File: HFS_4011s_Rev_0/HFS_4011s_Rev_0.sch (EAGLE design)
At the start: 56 parts, among them IC1 CP2104, J1 2X06, J2 2X12, J3 1X02, Q1 mmbt2222, Q2 mmbt2222, Q3 MMUN2133LT1G, SW2 KMR2, U1 TPS61090RSAR, U2 MCP73831T-2ACI/OT, U3 AD5693R, U4 LM3671MF-3.3/NOPB, X2 ESP32_WROOM32_SKINNY

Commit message: Added labels for FPAA IO. Still determining peripherals.
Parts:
- added J5: 1X02, HFS4011sCustom:1X02
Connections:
- new net E0: J2.23
- new net E1: J2.21
- new net E2: J2.19
- new net E3: J2.12
- new net E4: J2.10
- new net N$27: J2.14
- new net N$28: J2.16
- new net N$29: J2.18
- new net N$39: J2.13
- new net N$40: J2.15
- new net N$41: J2.17
- new net S0: J2.8
- new net S1: J1.8, J2.6
- new net S2: J2.4
- new net S3: J1.10, J2.2
- new net S4: J2.11
- new net S5: J1.12, J2.9
- new net S6: J2.7
- new net S7: J2.5
- new net S8: J2.3
- new net S9: J2.1
- new net W1: J2.24
- new net W3: J2.22
- new net W4: J2.20
- net 5.0V: now also J5.1
- net GND: now also J5.2
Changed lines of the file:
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@@
 <part name="R16" library="rcl" library_urn="urn:adsk.eagle:library:334" deviceset="R-US_" device="R0603" package3d_urn="urn:adsk.eagle:package:23555/2" value="5.1k"/>
 <part name="U$52" library="microbuilder" deviceset="3.3V" device=""/>
+<part name="J5" library="HFS4011sCustom" deviceset="1X02" device=""/>
+<part name="U$53" library="microbuilder" deviceset="5.0V" device=""/>
+<part name="U$54" library="microbuilder" deviceset="GND" device=""/>
 </parts>
 <sheets>
@@
 <instance part="R16" gate="G$1" x="190.5" y="195.58" rot="R90"/>
 <instance part="U$52" gate="G$1" x="142.24" y="177.8"/>
+<instance part="J5" gate="G$1" x="335.28" y="157.48"/>
+<instance part="U$53" gate="G$1" x="327.66" y="165.1"/>
+<instance part="U$54" gate="G$1" x="327.66" y="152.4"/>
 </instances>
 <busses>
@@
 <pinref part="U$50" gate="G$1" pin="GND"/>
 <wire x1="233.68" y1="129.54" x2="233.68" y2="127" width="0.1524" layer="91"/>
+</segment>
+<segment>
+<pinref part="J5" gate="G$1" pin="2"/>
+<pinref part="U$54" gate="G$1" pin="GND"/>
+<wire x1="330.2" y1="157.48" x2="327.66" y2="157.48" width="0.1524" layer="91"/>
+<wire x1="327.66" y1="157.48" x2="327.66" y2="154.94" width="0.1524" layer="91"/>
 </segment>
 </net>
@@
 <pinref part="C7" gate="G$1" pin="+"/>
 </segment>
+<segment>
+<pinref part="U$53" gate="G$1" pin="5.0V"/>
+<wire x1="327.66" y1="162.56" x2="327.66" y2="160.02" width="0.1524" layer="91"/>
+<pinref part="J5" gate="G$1" pin="1"/>
+<wire x1="327.66" y1="160.02" x2="330.2" y2="160.02" width="0.1524" layer="91"/>
+</segment>
 </net>
 <net name="N$10" class="0">
@@
 </segment>
 </net>
+<net name="S5" class="0">
+<segment>
+<pinref part="J1" gate="J$1" pin="12"/>
+<wire x1="327.66" y1="119.38" x2="335.28" y2="119.38" width="0.1524" layer="91"/>
+<label x="335.28" y="119.38" size="1.778" layer="95"/>
+<wire x1="335.28" y1="119.38" x2="337.82" y2="119.38" width="0.1524" layer="91"/>
+</segment>
+<segment>
+<pinref part="J2" gate="J$1" pin="9"/>
+<wire x1="337.82" y1="96.52" x2="327.66" y2="96.52" width="0.1524" layer="91"/>
+<label x="327.66" y="96.52" size="1.778" layer="95"/>
+</segment>
+</net>
+<net name="S3" class="0">
+<segment>
+<pinref part="J1" gate="J$1" pin="10"/>
+<wire x1="327.66" y1="121.92" x2="332.74" y2="121.92" width="0.1524" layer="91"/>
+<label x="335.28" y="121.92" size="1.778" layer="95"/>
+<wire x1="332.74" y1="121.92" x2="337.82" y2="121.92" width="0.1524" layer="91"/>
+</segment>
+<segment>
+<pinref part="J2" gate="J$1" pin="2"/>
+<wire x1="345.44" y1="106.68" x2="355.6" y2="106.68" width="0.1524" layer="91"/>
+<label x="353.06" y="106.68" size="1.778" layer="95"/>
+</segment>
+</net>
+<net name="S1" class="0">
+<segment>
+<pinref part="J1" gate="J$1" pin="8"/>
+<wire x1="327.66" y1="124.46" x2="332.74" y2="124.46" width="0.1524" layer="91"/>
+<label x="335.28" y="124.46" size="1.778" layer="95"/>
+<wire x1="332.74" y1="124.46" x2="337.82" y2="124.46" width="0.1524" layer="91"/>
+</segment>
+<segment>
+<pinref part="J2" gate="J$1" pin="6"/>
+<wire x1="345.44" y1="101.6" x2="355.6" y2="101.6" width="0.1524" layer="91"/>
+<label x="353.06" y="101.6" size="1.778" layer="95"/>
+</segment>
+</net>
+<net name="S2" class="0">
+<segment>
+<pinref part="J2" gate="J$1" pin="4"/>
+<wire x1="345.44" y1="104.14" x2="355.6" y2="104.14" width="0.1524" layer="91"/>
+<label x="353.06" y="104.14" size="1.778" layer="95"/>
+</segment>
+</net>
+<net name="S0" class="0">
+<segment>
+<pinref part="J2" gate="J$1" pin="8"/>
+<wire x1="345.44" y1="99.06" x2="355.6" y2="99.06" width="0.1524" layer="91"/>
+<label x="353.06" y="99.06" size="1.778" layer="95"/>
+</segment>
+</net>
+<net name="E4" class="0">
+<segment>
+<pinref part="J2" gate="J$1" pin="10"/>
+<wire x1="345.44" y1="96.52" x2="355.6" y2="96.52" width="0.1524" layer="91"/>
+<label x="353.06" y="96.52" size="1.778" layer="95"/>
+</segment>
+</net>
+<net name="E3" class="0">
+<segment>
+<pinref part="J2" gate="J$1" pin="12"/>
+<wire x1="345.44" y1="93.98" x2="355.6" y2="93.98" width="0.1524" layer="91"/>
+<label x="353.06" y="93.98" size="1.778" layer="95"/>
+</segment>
+</net>
+<net name="N$27" class="0">
+<segment>
+<pinref part="J2" gate="J$1" pin="14"/>
+<wire x1="345.44" y1="91.44" x2="355.6" y2="91.44" width="0.1524" layer="91"/>
+</segment>
+</net>
+<net name="N$28" class="0">
+<segment>
+<pinref part="J2" gate="J$1" pin="16"/>
+<wire x1="345.44" y1="88.9" x2="355.6" y2="88.9" width="0.1524" layer="91"/>
+</segment>
+</net>
+<net name="N$29" class="0">
+<segment>
+<pinref part="J2" gate="J$1" pin="18"/>
+<wire x1="345.44" y1="86.36" x2="355.6" y2="86.36" width="0.1524" layer="91"/>
+</segment>
+</net>
+<net name="W4" class="0">
+<segment>
+<pinref part="J2" gate="J$1" pin="20"/>
+<wire x1="345.44" y1="83.82" x2="355.6" y2="83.82" width="0.1524" layer="91"/>
+<label x="353.06" y="83.82" size="1.778" layer="95"/>
+</segment>
+</net>
+<net name="W3" class="0">
+<segment>
+<pinref part="J2" gate="J$1" pin="22"/>
+<wire x1="345.44" y1="81.28" x2="355.6" y2="81.28" width="0.1524" layer="91"/>
+<label x="353.06" y="81.28" size="1.778" layer="95"/>
+</segment>
+</net>
+<net name="W1" class="0">
+<segment>
+<pinref part="J2" gate="J$1" pin="24"/>
+<wire x1="345.44" y1="78.74" x2="355.6" y2="78.74" width="0.1524" layer="91"/>
+<label x="353.06" y="78.74" size="1.778" layer="95"/>
+</segment>
+</net>
+<net name="S9" class="0">
+<segment>
+<pinref part="J2" gate="J$1" pin="1"/>
+<wire x1="337.82" y1="106.68" x2="327.66" y2="106.68" width="0.1524" layer="91"/>
+<label x="327.66" y="106.68" size="1.778" layer="95"/>
+</segment>
+</net>
+<net name="S8" class="0">
+<segment>
+<pinref part="J2" gate="J$1" pin="3"/>
+<wire x1="337.82" y1="104.14" x2="327.66" y2="104.14" width="0.1524" layer="91"/>
+<label x="327.66" y="104.14" size="1.778" layer="95"/>
+</segment>
+</net>
+<net name="S7" class="0">
+<segment>
+<pinref part="J2" gate="J$1" pin="5"/>
+<wire x1="337.82" y1="101.6" x2="327.66" y2="101.6" width="0.1524" layer="91"/>
+<label x="327.66" y="101.6" size="1.778" layer="95"/>
+</segment>
+</net>
+<net name="S6" class="0">
+<segment>
+<pinref part="J2" gate="J$1" pin="7"/>
+<wire x1="337.82" y1="99.06" x2="327.66" y2="99.06" width="0.1524" layer="91"/>
+<label x="327.66" y="99.06" size="1.778" layer="95"/>
+</segment>
+</net>
+<net name="S4" class="0">
+<segment>
+<pinref part="J2" gate="J$1" pin="11"/>
+<wire x1="337.82" y1="93.98" x2="327.66" y2="93.98" width="0.1524" layer="91"/>
+<label x="327.66" y="93.98" size="1.778" layer="95"/>
+</segment>
+</net>
+<net name="N$39" class="0">
+<segment>
+<pinref part="J2" gate="J$1" pin="13"/>
+<wire x1="337.82" y1="91.44" x2="327.66" y2="91.44" width="0.1524" layer="91"/>
+</segment>
+</net>
+<net name="N$40" class="0">
+<segment>
+<pinref part="J2" gate="J$1" pin="15"/>
+<wire x1="337.82" y1="88.9" x2="327.66" y2="88.9" width="0.1524" layer="91"/>
+</segment>
+</net>
+<net name="N$41" class="0">
+<segment>
+<pinref part="J2" gate="J$1" pin="17"/>
+<wire x1="337.82" y1="86.36" x2="327.66" y2="86.36" width="0.1524" layer="91"/>
+</segment>
+</net>
+<net name="E2" class="0">
+<segment>
+<pinref part="J2" gate="J$1" pin="19"/>
+<wire x1="337.82" y1="83.82" x2="327.66" y2="83.82" width="0.1524" layer="91"/>
+<label x="327.66" y="83.82" size="1.778" layer="95"/>
+</segment>
+</net>
+<net name="E1" class="0">
+<segment>
+<pinref part="J2" gate="J$1" pin="21"/>
+<wire x1="337.82" y1="81.28" x2="327.66" y2="81.28" width="0.1524" layer="91"/>
+<label x="327.66" y="81.28" size="1.778" layer="95"/>
+</segment>
+</net>
+<net name="E0" class="0">
+<segment>
+<pinref part="J2" gate="J$1" pin="23"/>
+<wire x1="337.82" y1="78.74" x2="327.66" y2="78.74" width="0.1524" layer="91"/>
+<label x="327.66" y="78.74" size="1.778" layer="95"/>
+</segment>
+</net>

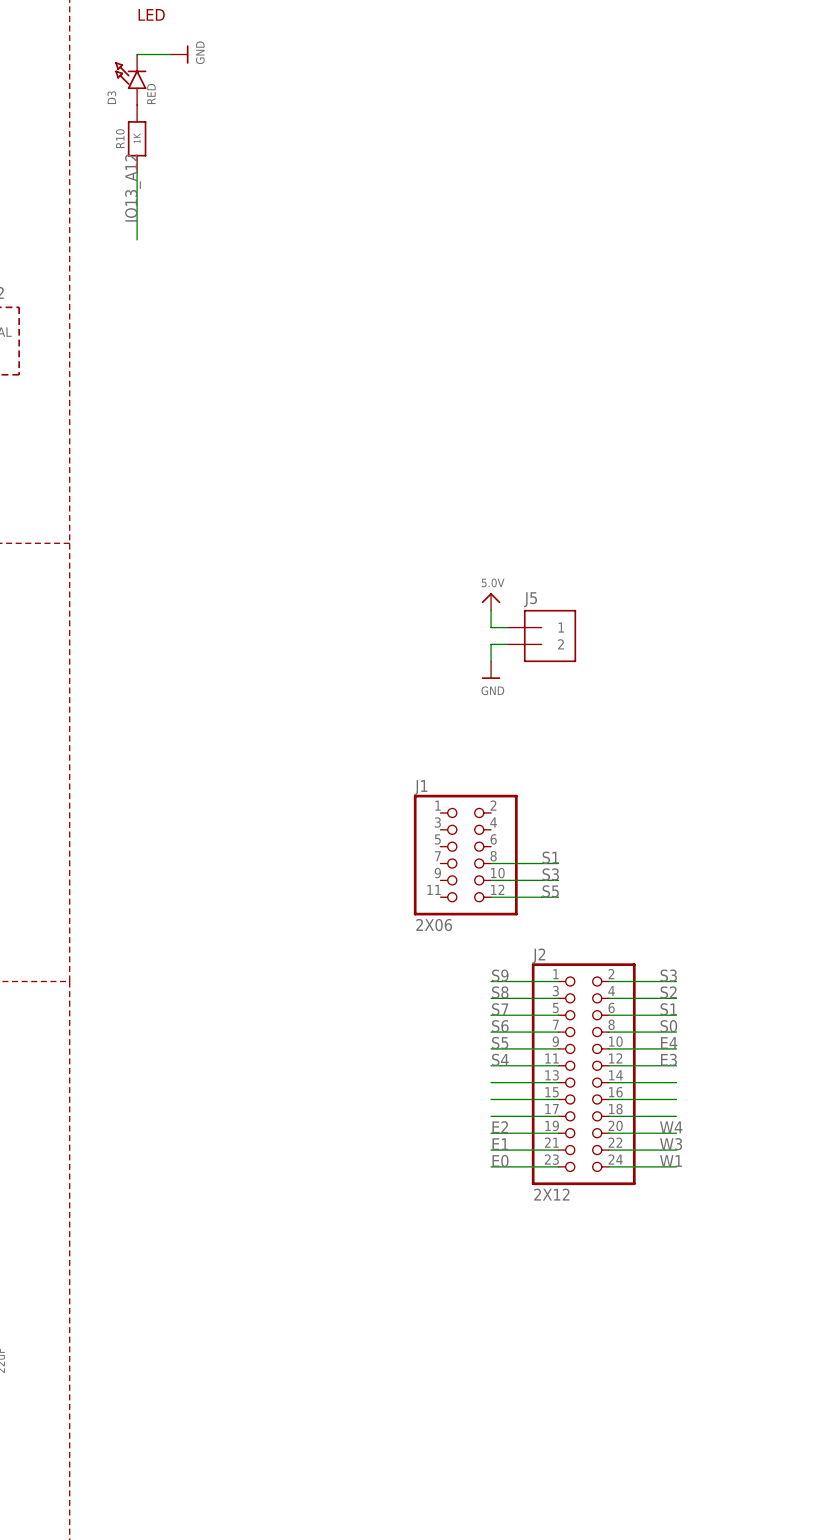
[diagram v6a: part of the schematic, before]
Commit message: Working on IO. Need to get bigger connector for IO!
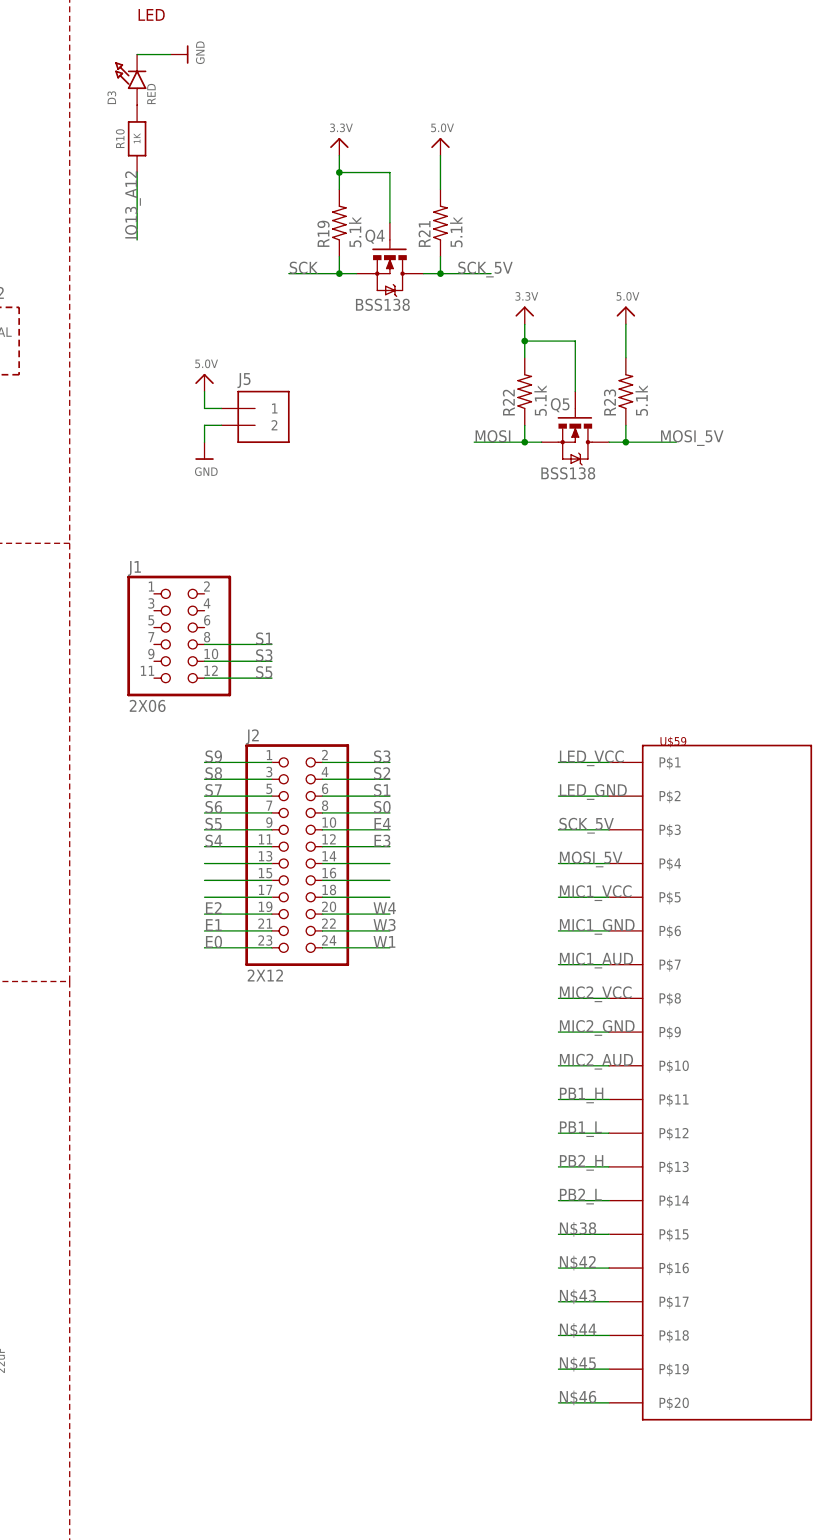
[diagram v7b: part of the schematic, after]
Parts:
- added Q4, Q5: BSS138, SparkFun:MOSFET-NCHANNELSMD
- added R19, R21, R22, R23: 5.1k, rcl:R-US_R0603
- added U$59: (no value), HFS4011sCustom:MOLEX_IGRID_10X2CONNECTOR
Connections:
- new net LED_GND: U$59.P$2
- new net LED_VCC: U$59.P$1
- new net MIC1_AUD: U$59.P$7
- new net MIC1_GND: U$59.P$6
- new net MIC1_VCC: U$59.P$5
- new net MIC2_AUD: U$59.P$10
- new net MIC2_GND: U$59.P$9
- new net MIC2_VCC: U$59.P$8
- new net MOSI_5V: Q5.D, R23.1, U$59.P$4
- new net N$38: U$59.P$15
- new net N$42: U$59.P$16
- new net N$43: U$59.P$17
- new net N$44: U$59.P$18
- new net N$45: U$59.P$19
- new net N$46: U$59.P$20
- new net PB1_H: U$59.P$11
- new net PB1_L: U$59.P$12
- new net PB2_H: U$59.P$13
- new net PB2_L: U$59.P$14
- new net SCK_5V: Q4.D, R21.1, U$59.P$3
- net 3.3V: now also Q4.G, Q5.G, R19.2, R22.2
- net 5.0V: now also R21.2, R23.2
- net MOSI: now also Q5.S, R22.1
- net SCK: now also Q4.S, R19.1
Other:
- moved on the sheet: J1, J2, J5

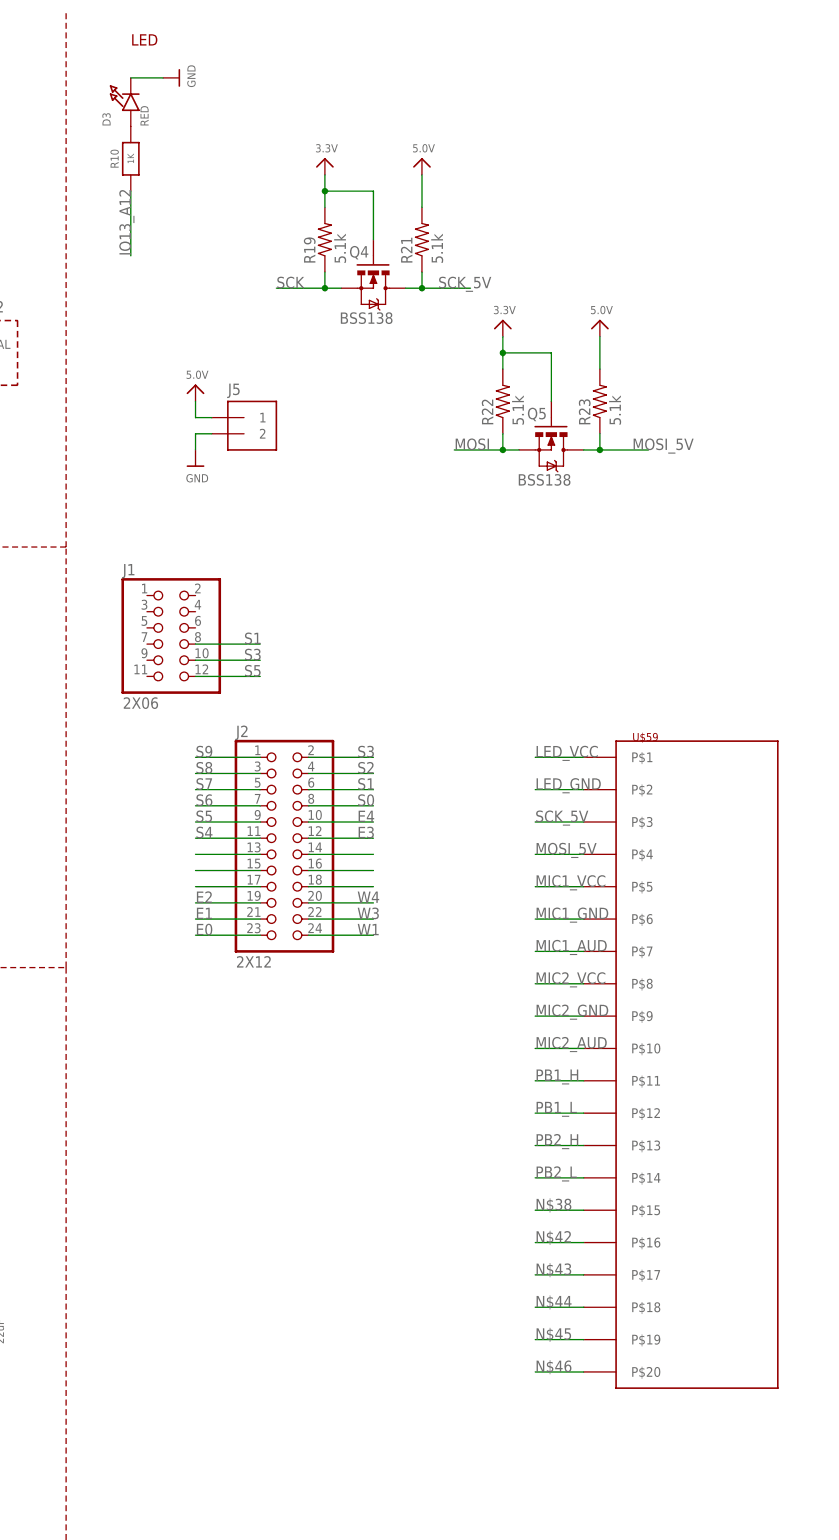
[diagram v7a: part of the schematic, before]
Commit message: Addded peripherals. Still need to connect IO from microcontroller to connector.
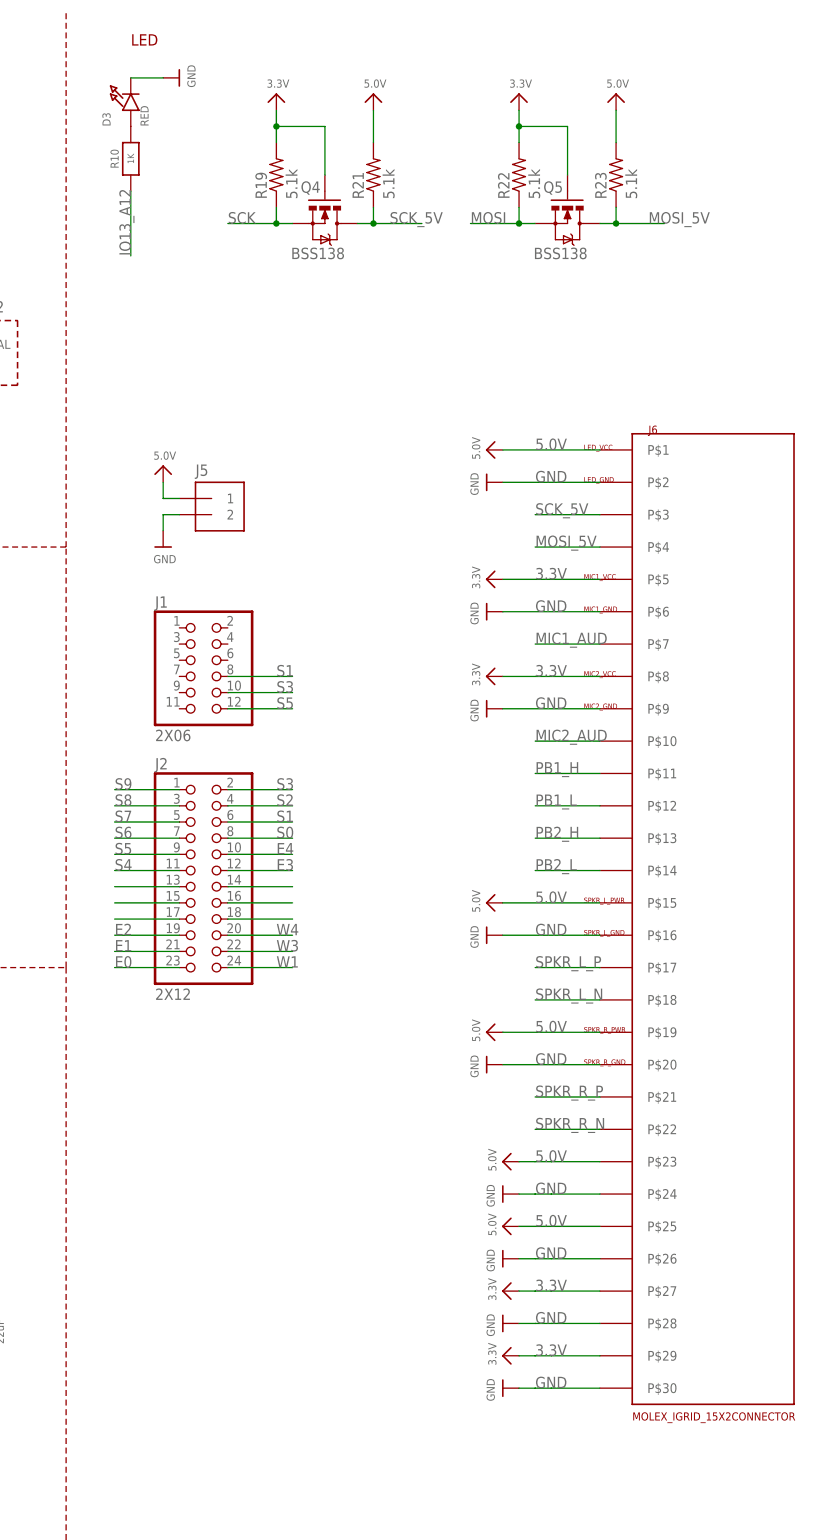
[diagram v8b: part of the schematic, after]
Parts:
- removed U$59: (no value), HFS4011sCustom:MOLEX_IGRID_10X2CONNECTOR
- added J6: MOLEX_IGRID_15X2CONNECTOR, HFS4011sCustom:MOLEX_IGRID_15X2CONNECTOR
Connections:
- removed net LED_GND: U$59.P$2
- removed net LED_VCC: U$59.P$1
- removed net MIC1_GND: U$59.P$6
- removed net MIC1_VCC: U$59.P$5
- removed net MIC2_GND: U$59.P$9
- removed net MIC2_VCC: U$59.P$8
- removed net N$38: U$59.P$15
- removed net N$42: U$59.P$16
- removed net N$43: U$59.P$17
- removed net N$44: U$59.P$18
- removed net N$45: U$59.P$19
- removed net N$46: U$59.P$20
- new net SPKR_L_N: J6.P$18
- new net SPKR_L_P: J6.P$17
- new net SPKR_R_N: J6.P$22
- new net SPKR_R_P: J6.P$21
- net 3.3V: now also J6.P$27, J6.P$29, J6.P$5, J6.P$8
- net 5.0V: now also J6.P$1, J6.P$15, J6.P$19, J6.P$23, J6.P$25
- net GND: now also J6.P$16, J6.P$2, J6.P$20, J6.P$24, J6.P$26, J6.P$28, J6.P$30, J6.P$6, J6.P$9
- net MIC1_AUD: now also J6.P$7; no longer U$59.P$7
- net MIC2_AUD: now also J6.P$10; no longer U$59.P$10
- net MOSI_5V: now also J6.P$4; no longer U$59.P$4
- net PB1_H: now also J6.P$11; no longer U$59.P$11
- net PB1_L: now also J6.P$12; no longer U$59.P$12
- net PB2_H: now also J6.P$13; no longer U$59.P$13
- net PB2_L: now also J6.P$14; no longer U$59.P$14
- net SCK_5V: now also J6.P$3; no longer U$59.P$3
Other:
- note added: "LED_GND"
- note added: "LED_VCC"
- note added: "MIC1_GND"
- note added: "MIC1_VCC"
- note added: "MIC2_GND"
- note added: "MIC2_VCC"
- note added: "SPKR_L_GND"
- note added: "SPKR_L_PWR"
- note added: "SPKR_R_GND"
- note added: "SPKR_R_PWR"
- moved on the sheet: J1, J2, J5, Q4, Q5, R19, R21, R22, R23
